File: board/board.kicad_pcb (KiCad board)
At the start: 2 copper layers, 21 x 13 mm, 7 parts, among them J1 001_I2C, J2 001_I2C, U1 SHT30-DIS

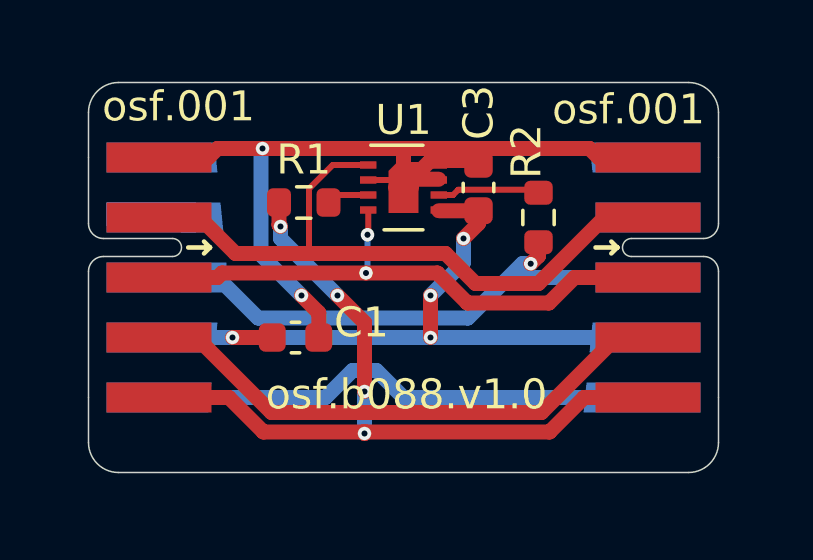
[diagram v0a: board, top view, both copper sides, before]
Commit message: used new normal rounded corners and added ground planes
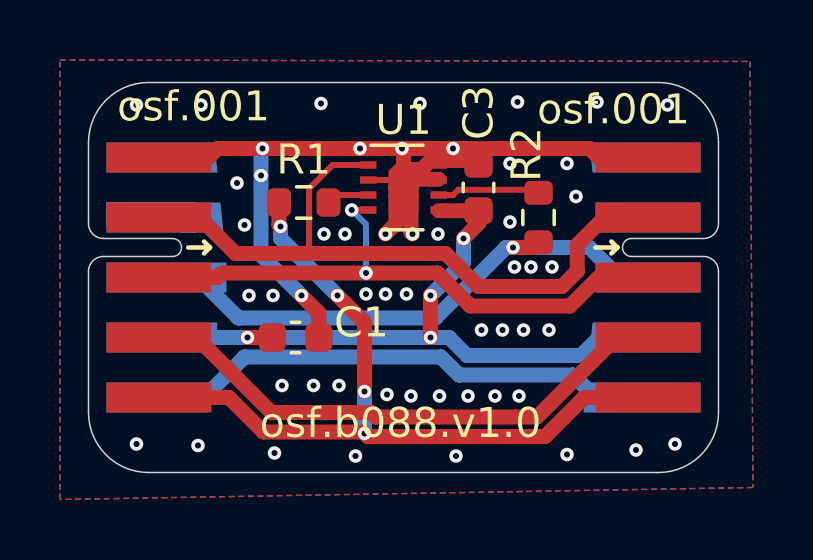
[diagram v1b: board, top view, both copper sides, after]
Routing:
- net GND: track 30.5 -> 34.0 mm, vias 2 -> 53
- net /sensor/SCL: track 19.3 -> 20.1 mm
- net /sensor/SDA: track 22.6 -> 23.2 mm
- added copper zone on B.Cu, net GND
- added copper zone on F.Cu, net GND
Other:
- outline, holes or cut-outs redrawn

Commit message: added LCSC part numbers
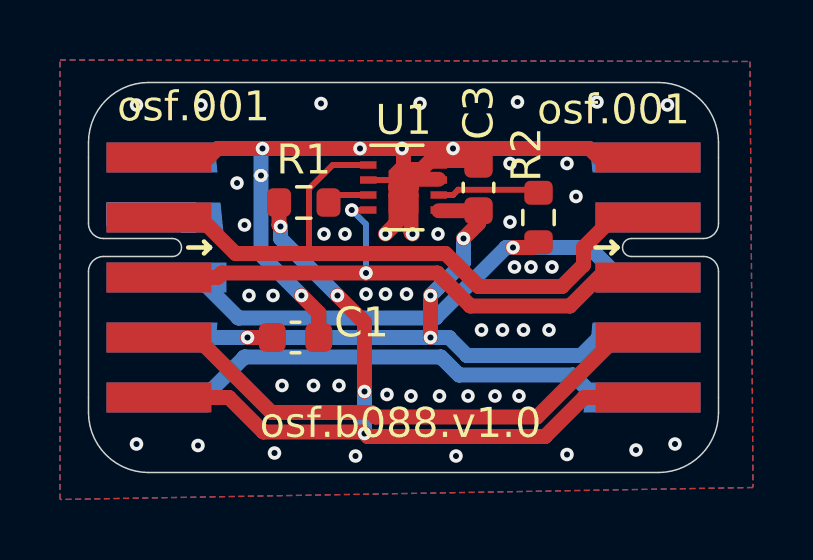
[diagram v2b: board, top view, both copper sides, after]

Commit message: updated I2C connector to current standard
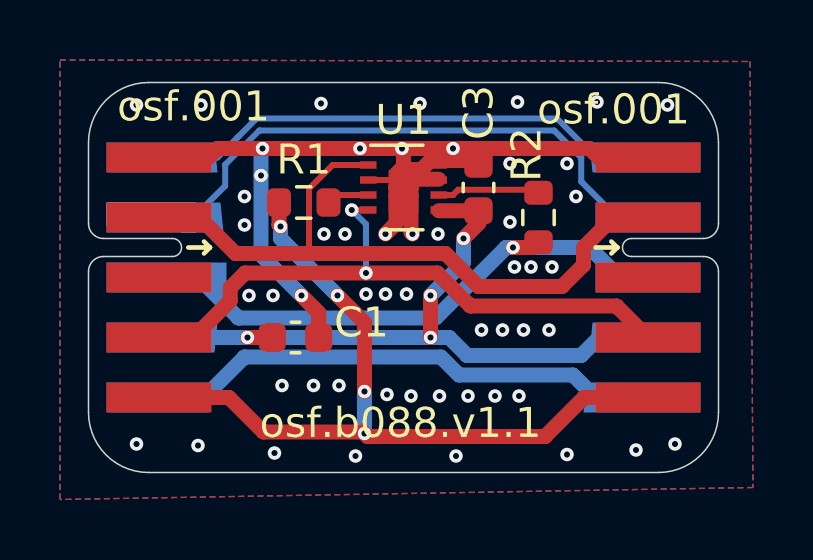
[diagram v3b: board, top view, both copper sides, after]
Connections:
- J1 pad 3: /sensor/SCL -> unconnected-(J1-N/C-Pad3)
- J1 pad 4: Net-(J1-Pad4) -> /sensor/SCL
- J1 pad 6: (no net) -> Net-(J1-CS/EN)
- J1 pad 7: (no net) -> Net-(J1-status)
- J2 pad 3: /sensor/SCL -> unconnected-(J2-N/C-Pad3)
- J2 pad 4: Net-(J1-Pad4) -> /sensor/SCL
- J2 pad 6: (no net) -> Net-(J1-CS/EN)
- J2 pad 7: (no net) -> Net-(J1-status)
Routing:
- net Net-(J1-status): track 0.00 -> 19.8 mm
- net Net-(J1-Pad4): track 18.5 -> 0.00 mm
- net Net-(J1-CS/EN): track 0.00 -> 17.3 mm
- net /sensor/SCL: track 20.1 -> 21.2 mm
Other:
- board text added: "osf.b088.v1.1"
- board text removed: "osf.b088.v1.0"
